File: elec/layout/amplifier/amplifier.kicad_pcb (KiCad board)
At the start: 2 copper layers, 29 parts, among them U1 _Texas_Instruments_TAS5825MRH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

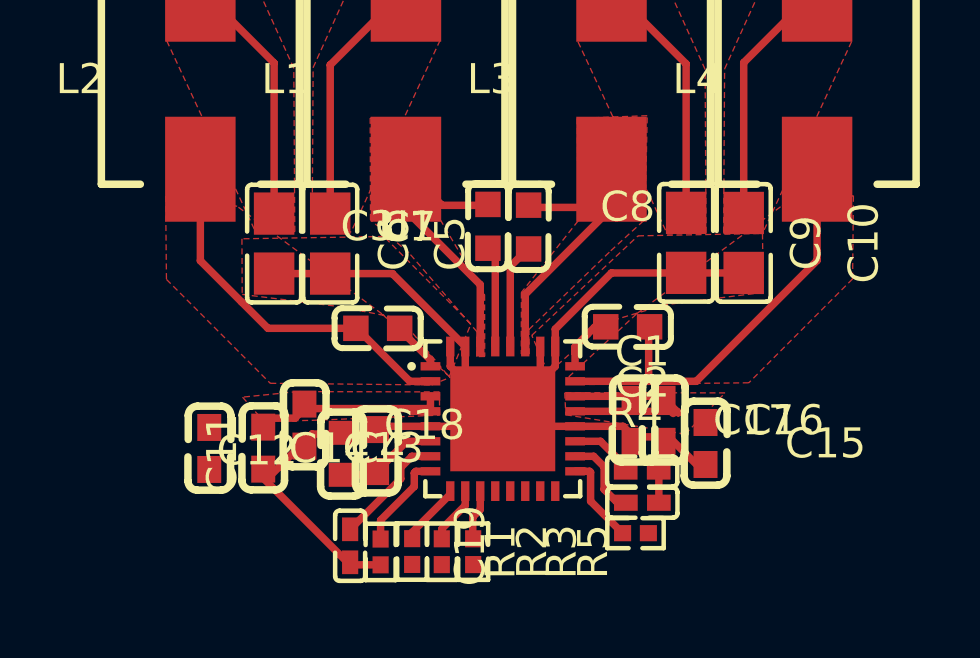
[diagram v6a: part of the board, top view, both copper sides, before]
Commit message: Don't update PCB files
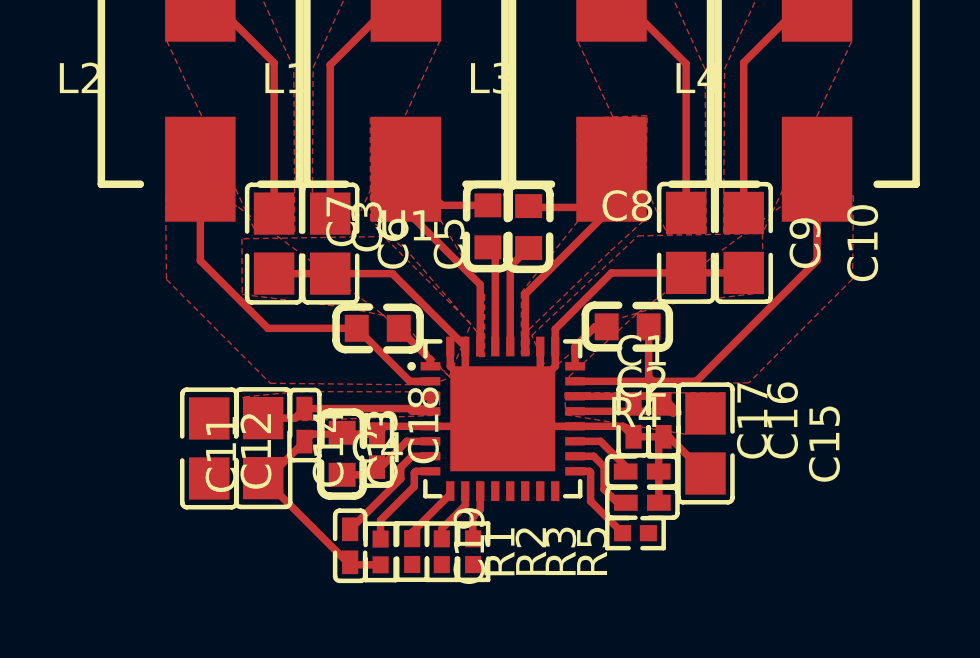
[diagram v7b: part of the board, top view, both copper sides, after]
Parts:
- C1, C19, C2: value 1µF ±10% 10V X5R -> 1µF ±10% 25V X5R
- C11: value 100nF ±10% 50V X7R -> 4.7µF ±10% 16V X5R
- C12, C16, C17, C18: value 100nF ±10% 50V X7R -> 100nF ±10% 16V X7R; footprint lcsc:C0603 -> lcsc:C0402
- C13, C14, C15: value 100nF ±10% 50V X7R -> 22µF ±20% 25V X5R; footprint lcsc:C0603 -> lcsc:C0805
- C3, C4, C7, C8: footprint lcsc:CAP-SMD_L1.6-W0.8-3 -> lcsc:C0603
- L1, L2, L3, L4: value 10µH ±20% infHz 4.5A 68mΩ -> 10µH ±20% 4.5A 68mΩ
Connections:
- net hv-1 renamed mute-hv
- net hv-3 renamed fault-hv
- net hv-4 renamed pdn-hv
- C1 pad 1: net-10 -> net-6
- C1 pad 2: net-4 -> net
- C10 pad 1: signal-2 -> signal-1
- C10 pad 2: net-4 -> net
- C11 pad 1: hv-2 -> hv
- C11 pad 2: net-4 -> net
- C12 pad 1: hv-2 -> hv
- C12 pad 2: net-4 -> net
- C13 pad 1: net-5 -> net-4
- C13 pad 2: net-4 -> net
- C14 pad 1: net-5 -> net-4
- C14 pad 2: net-4 -> net
- C15 pad 1: net-5 -> net-4
- C15 pad 2: net-4 -> net
- C16 pad 1: net-5 -> net-4
- C16 pad 2: net-4 -> net
- C17 pad 1: net-5 -> net-4
- C17 pad 2: net-4 -> net
- C18 pad 1: net-5 -> net-4
- C18 pad 2: net-4 -> net
- C19 pad 1: net-11 -> net-12
- C19 pad 2: net-4 -> net
- C2 pad 1: net-3 -> net-5
- C2 pad 2: net-4 -> net
- C3 pad 1: net-14 -> net-10
- C3 pad 2: net-9 -> net-8
- C4 pad 1: net-7 -> net-13
- C4 pad 2: net-8 -> net-14
- C5 pad 1: signal-1 -> signal
- C5 pad 2: net-4 -> net
- C6 pad 1: signal-3 -> signal-2
- C6 pad 2: net-4 -> net
- C7 pad 1: net -> net-1
- C7 pad 2: net-1 -> net-2
- C8 pad 1: net-16 -> net-11
- C8 pad 2: net-13 -> net-7
- C9 pad 1: signal -> signal-3
- C9 pad 2: net-4 -> net
- L1 pad 1: net-9 -> net-8
- L1 pad 2: signal-1 -> signal
- L2 pad 1: net-8 -> net-14
- L2 pad 2: signal-3 -> signal-2
- L3 pad 1: net-1 -> net-2
- L3 pad 2: signal -> signal-3
- L4 pad 1: net-13 -> net-7
- L4 pad 2: signal-2 -> signal-1
- R1 pad 1: net-12 -> net-3
- R1 pad 2: net-4 -> net
- R2 pad 1: net-17 -> net-15
- R3 pad 1: net-6 -> net-16
- R4 pad 1: net-15 -> net-17
- R5 pad 1: net-2 -> net-9
- R5 pad 2: hv -> warn-hv
- U1 pad 1: net-7 -> net-13
- U1 pad 10: net-6 -> net-16
- U1 pad 11: net-2 -> net-9
- U1 pad 17: net-15 -> net-17
- U1 pad 18: net-3 -> net-5
- U1 pad 19: net-10 -> net-6
- U1 pad 2: net-8 -> net-14
- U1 pad 20: net-4 -> net
- U1 pad 21: net-5 -> net-4
- U1 pad 22: net-5 -> net-4
- U1 pad 23: net-13 -> net-7
- U1 pad 24: net-16 -> net-11
- U1 pad 25: net-4 -> net
- U1 pad 26: net-4 -> net
- U1 pad 27: net-1 -> net-2
- U1 pad 28: net -> net-1
- U1 pad 29: net-14 -> net-10
- U1 pad 3: net-5 -> net-4
- U1 pad 30: net-9 -> net-8
- U1 pad 31: net-4 -> net
- U1 pad 32: net-4 -> net
- U1 pad 33: net-4 -> net
- U1 pad 4: net-5 -> net-4
- U1 pad 5: net-4 -> net
- U1 pad 6: hv-2 -> hv
- U1 pad 7: net-11 -> net-12
- U1 pad 8: net-12 -> net-3
- U1 pad 9: net-17 -> net-15

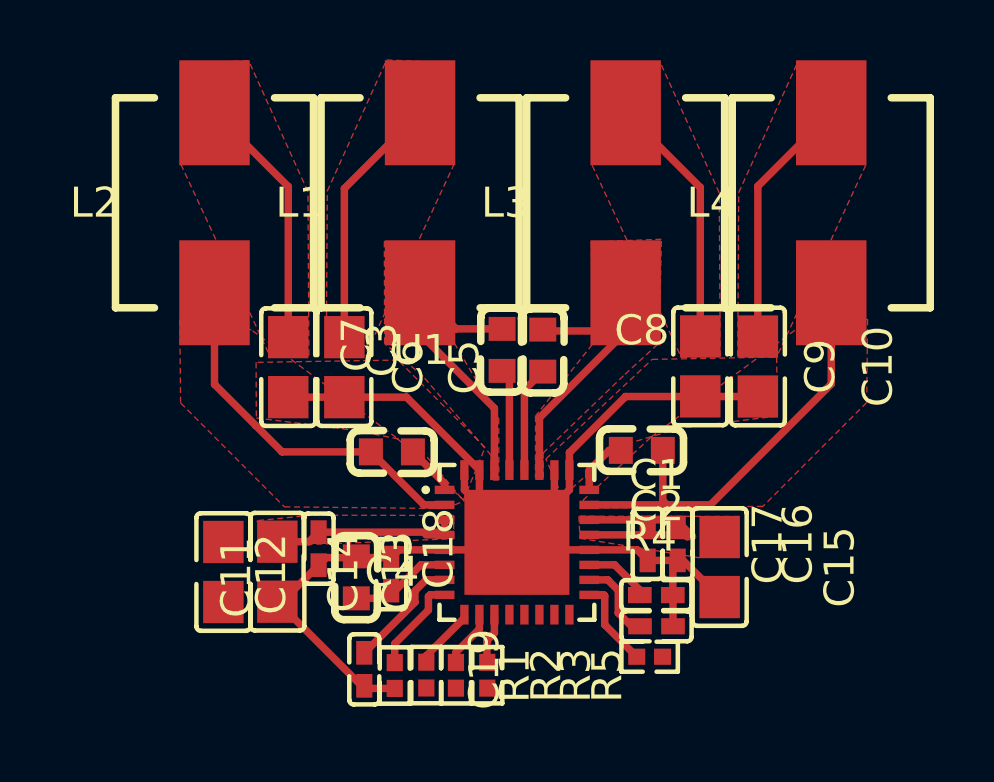
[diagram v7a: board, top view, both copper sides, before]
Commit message: Update PCB version to kicad9; Disable non-existing builds
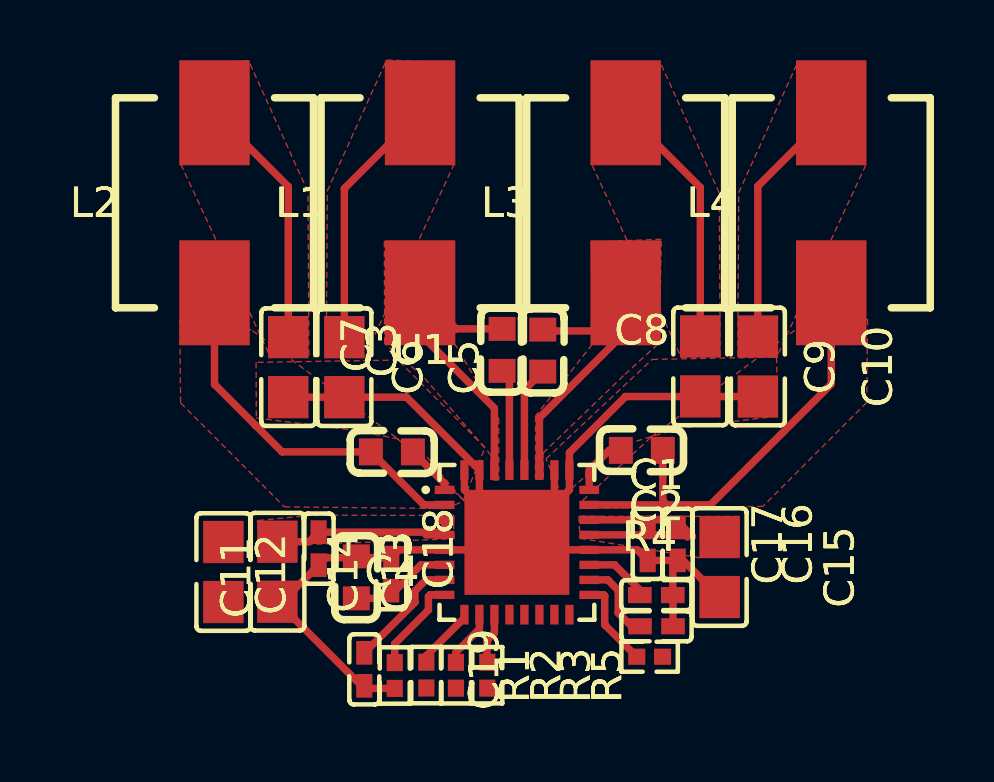
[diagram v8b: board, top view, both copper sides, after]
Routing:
- net (no net): track 65.3 -> 0.00 mm
- net net: track 2.78 -> 50.8 mm
- net net-5: track 14.6 -> 2.78 mm
- net net-7: track 4.03 -> 14.6 mm
- net net-14: track 3.41 -> 12.4 mm
- net net-2: track 3.34 -> 10.8 mm
- net net-12: track 10.2 -> 4.03 mm
- net net-17: track 0.00 -> 3.34 mm
- net net-4: track 12.4 -> 14.5 mm
- net net-16: track 0.00 -> 1.91 mm
- net net-3: track 1.70 -> 3.34 mm
- net net-1: track 2.20 -> 3.53 mm
- net net-15: track 3.34 -> 2.11 mm
- net net-8: track 10.8 -> 10.2 mm
- net net-6: track 1.70 -> 2.20 mm
